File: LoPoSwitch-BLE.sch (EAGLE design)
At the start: 12 parts, among them Q1 2.5A/30V

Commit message: Restyle Board with SeedStudio Elements
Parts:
- removed C1, C2: 22uF, SparkFun-Capacitors:22UF-16V-20%-(1210)
- removed FREQ_RESONATOR: 16MHZ, SparkFun-FreqCtrl:RESONATOR16MHZ
- removed Q1: 2.5A/30V, SparkFun-DiscreteSemi:MOSFET-PCHANNELDMG2307L
- removed RESET.BUTTON: BUTTON-CONDUCTIVESMD, SparkFun-Electromechanical:BUTTON-CONDUCTIVESMD
- removed U$2: RELAY-2G5Q, SparkFun-Electromechanical:RELAY-2G5Q
- added CAPACITOR-16HZ: 16MHZ, Seeed-Crystal Oscillator:DIP-CRYSTAL-16MHZ-18PF-30PPM-50R(HC49US)
- added CAPACITOR-22PF-1, CAPACITOR-22PF-2, CAPACITOR-22PF-3, CAPACITOR-22PF-4: 100uf, Seeed-Capacitor:DIP-ALUMINUM-47UF-16V(D5-H7MM)
- added D1: 504BW, Seeed-LED:DIP-LED-BLUE-BLUE(2P-D5MM)
- added K1: (no value), Seeed-Relay:RELAY-HLS8L-DC5V-S-CHLS8L-DC5V-S-C
- added R1, R2, R6: 220R, Seeed-Resistor:DIP-RES-220R-5%-1/4W(PR-D2.3XL6.5MM)
- added R3: 1M, Seeed-Resistor:DIP-RES-1M-5%-1/4W(PR-D2.3XL6.5MM)
- added R4: 100K, Seeed-Resistor:DIP-RES-100K-5%-1/6W(PR-D1.8XL3.3MM)
- added RED-LED, RED-LED1: SR302DC, Seeed-LED:DIP-LED-RED-RED(2P-D3MM)
- added RESET-BUTTON: TS-1101F, Seeed-Switch:DIP-BUTTON(2P-6.0X3.0X4.3MM)-TS-1101F
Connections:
- removed net N$4: 12VO.1, Q1.S
- new net N$7: D1.+, R1.1
- new net N$8: R2.1, RED-LED.+
- new net N$9: ATMEGA328.P$22
- new net PD6: ATMEGA328.P$12, R6.1
- net 12VIN: now also 12VIN.2, K1.NO; no longer 12VIN.1, Q1.D
- net 3.3VIN: no longer C2.2
- net 5VIN: now also ATMEGA328.P$20, ATMEGA328.P$21, CAPACITOR-22PF-4.-, R2.2, R3.2; no longer C1.2
- net ARDUINO.D3: now also ATMEGA328.P$4; no longer Q1.G
- net GND: now also 12VIN.1, 12VO.1, ATMEGA328.P$10, ATMEGA328.P$9, RED-LED.-, RED-LED1.-, RESET-BUTTON.1; no longer 12VIN.2, 12VO.2, FREQ_RESONATOR.2, RESET.BUTTON.1
- net N$1: now also 12VO.2; no longer ATMEGA328.P$9, FREQ_RESONATOR.1
- net N$2: now also R6.2, RED-LED1.+; no longer ATMEGA328.P$10, FREQ_RESONATOR.3
- net N$3: now also RESET-BUTTON.2; no longer RESET.BUTTON.2
- net N$5: now also CAPACITOR-22PF-4.+; no longer C1.1
- net N$6: no longer C2.1
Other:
- moved on the sheet: 12VO

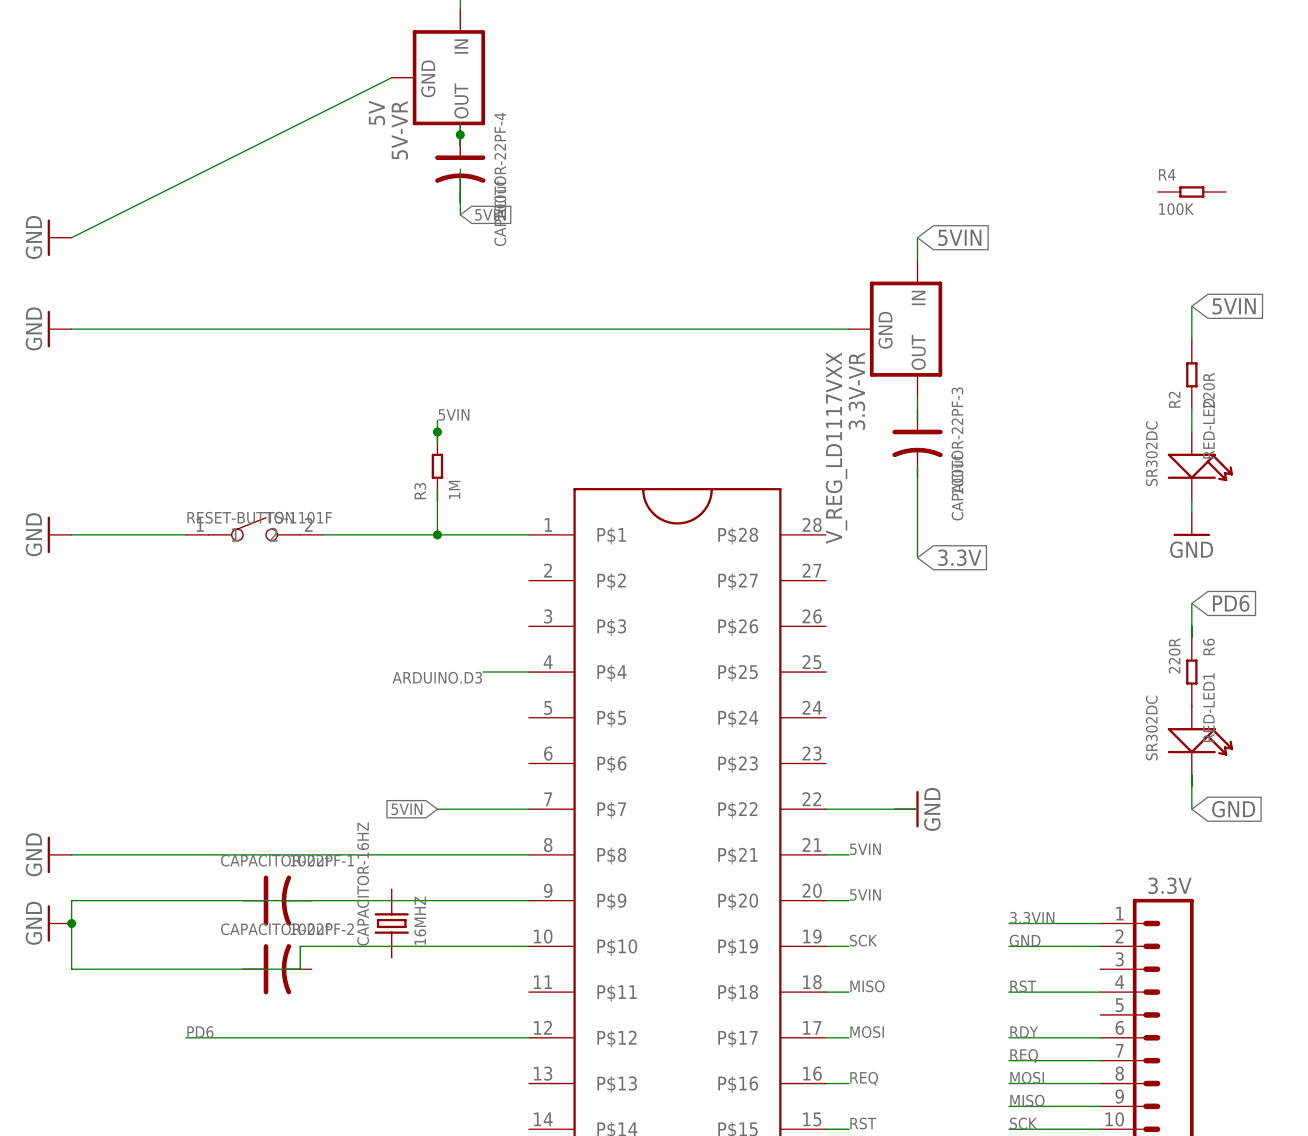
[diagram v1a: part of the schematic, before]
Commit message: Change Grid to 0.05 inch
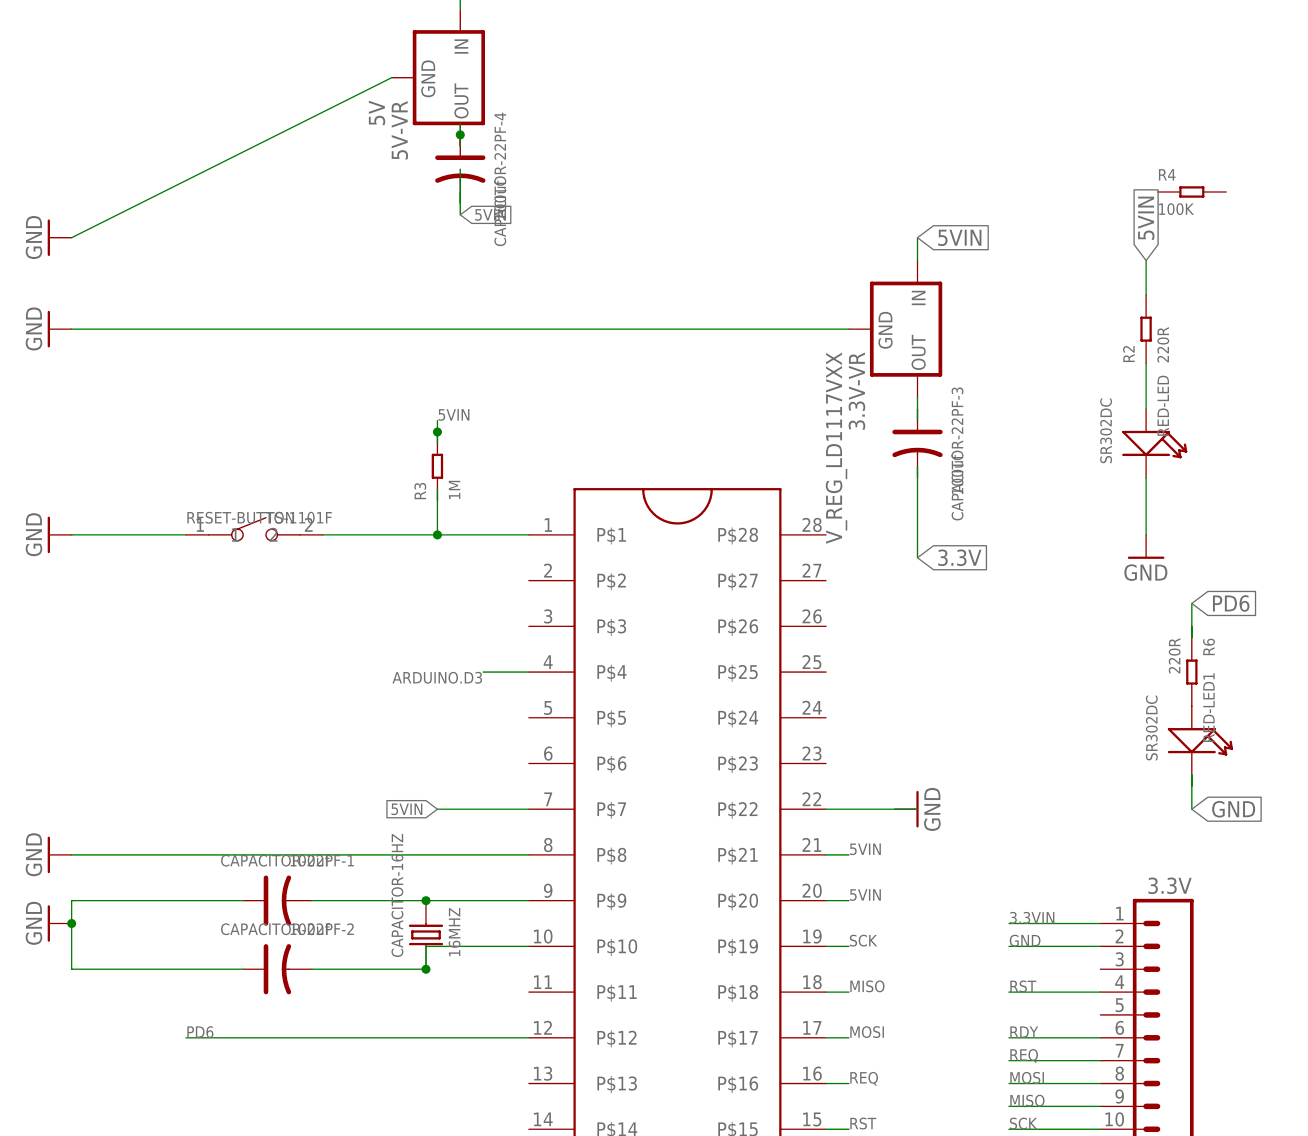
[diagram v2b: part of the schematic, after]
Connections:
- new net N$10: ATMEGA328.P$9, CAPACITOR-16HZ.2, CAPACITOR-22PF-1.-
- new net N$11: ATMEGA328.P$10, CAPACITOR-16HZ.1, CAPACITOR-22PF-2.-
- net GND: now also CAPACITOR-22PF-1.+, CAPACITOR-22PF-2.+; no longer ATMEGA328.P$10, ATMEGA328.P$9
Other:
- moved on the sheet: CAPACITOR-16HZ, R2, RED-LED
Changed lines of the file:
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@@
 <setting verticaltext="up"/>
 </settings>
-<grid distance="0.1" unitdist="inch" unit="inch" style="dots" multiple="1" display="yes" altdistance="0.01" altunitdist="inch" altunit="inch"/>
+<grid distance="0.05" unitdist="inch" unit="inch" style="lines" multiple="1" display="yes" altdistance="0.025" altunitdist="inch" altunit="inch"/>
 <layers>
 <layer number="1" name="Top" color="4" fill="1" visible="no" active="no"/>
@@
 <instance part="GND3" gate="1" x="119.38" y="-48.26" rot="R90"/>
 <instance part="GND8" gate="1" x="132.08" y="-111.76"/>
-<instance part="GND9" gate="1" x="149.86" y="-17.78"/>
+<instance part="GND9" gate="1" x="144.78" y="-20.32"/>
 <instance part="RESET-BUTTON" gate="G$1" x="45.72" y="-17.78"/>
-<instance part="CAPACITOR-16HZ" gate="G$1" x="60.96" y="-60.96" rot="R90"/>
+<instance part="CAPACITOR-16HZ" gate="G$1" x="64.77" y="-62.23" rot="R90"/>
 <instance part="CAPACITOR-22PF-1" gate="G$1" x="48.26" y="-58.42"/>
 <instance part="CAPACITOR-22PF-2" gate="G$1" x="48.26" y="-66.04"/>
 <instance part="CAPACITOR-22PF-3" gate="G$1" x="119.38" y="-7.62" rot="R270"/>
 <instance part="R6" gate="G$1" x="149.86" y="-33.02" rot="R270"/>
-<instance part="RED-LED" gate="G$1" x="149.86" y="-10.16" rot="R270"/>
+<instance part="RED-LED" gate="G$1" x="144.78" y="-7.62" rot="R270"/>
 <instance part="CAPACITOR-22PF-4" gate="G$1" x="68.58" y="22.86" rot="R270"/>
 <instance part="R3" gate="G$1" x="66.04" y="-10.16" rot="R90"/>
@@
 <instance part="GND11" gate="1" x="66.04" y="-124.46"/>
 <instance part="RED-LED1" gate="G$1" x="149.86" y="-40.64" rot="R270"/>
-<instance part="R2" gate="G$1" x="149.86" y="0" rot="R90"/>
+<instance part="R2" gate="G$1" x="144.78" y="5.08" rot="R90"/>
 <instance part="R4" gate="G$1" x="149.86" y="20.32"/>
 </instances>
@@
 </segment>
 <segment>
-<pinref part="ATMEGA328" gate="G$1" pin="P$9"/>
-<pinref part="GND2" gate="1" pin="GND"/>
-<wire x1="76.2" y1="-58.42" x2="25.4" y2="-58.42" width="0.1524" layer="91"/>
-<wire x1="25.4" y1="-58.42" x2="25.4" y2="-60.96" width="0.1524" layer="91"/>
-<pinref part="ATMEGA328" gate="G$1" pin="P$10"/>
-<wire x1="76.2" y1="-63.5" x2="50.8" y2="-63.5" width="0.1524" layer="91"/>
-<wire x1="50.8" y1="-63.5" x2="50.8" y2="-66.04" width="0.1524" layer="91"/>
-<wire x1="50.8" y1="-66.04" x2="25.4" y2="-66.04" width="0.1524" layer="91"/>
-<wire x1="25.4" y1="-66.04" x2="25.4" y2="-60.96" width="0.1524" layer="91"/>
-<junction x="25.4" y="-60.96"/>
-</segment>
-<segment>
 <pinref part="GND1" gate="1" pin="GND"/>
 <pinref part="12VO" gate="G$1" pin="1"/>
@@
 <pinref part="3.3V-VR" gate="G$1" pin="GND"/>
 <wire x1="25.4" y1="5.08" x2="111.76" y2="5.08" width="0.1524" layer="91"/>
-</segment>
-<segment>
-<pinref part="GND9" gate="1" pin="GND"/>
-<pinref part="RED-LED" gate="G$1" pin="-"/>
-<wire x1="149.86" y1="-13.97" x2="149.86" y2="-15.24" width="0.1524" layer="91"/>
 </segment>
 <segment>
@@
 <pinref part="RED-LED1" gate="G$1" pin="-"/>
 <wire x1="149.86" y1="-44.45" x2="149.86" y2="-45.72" width="0.1524" layer="91"/>
+</segment>
+<segment>
+<pinref part="RED-LED" gate="G$1" pin="-"/>
+<pinref part="GND9" gate="1" pin="GND"/>
+<wire x1="144.78" y1="-11.43" x2="144.78" y2="-17.78" width="0.1524" layer="91"/>
+</segment>
+<segment>
+<pinref part="CAPACITOR-22PF-1" gate="G$1" pin="+"/>
+<pinref part="GND2" gate="1" pin="GND"/>
+<wire x1="44.45" y1="-58.42" x2="25.4" y2="-58.42" width="0.1524" layer="91"/>
+<wire x1="25.4" y1="-58.42" x2="25.4" y2="-60.96" width="0.1524" layer="91"/>
+<pinref part="CAPACITOR-22PF-2" gate="G$1" pin="+"/>
+<wire x1="44.45" y1="-66.04" x2="25.4" y2="-66.04" width="0.1524" layer="91"/>
+<wire x1="25.4" y1="-66.04" x2="25.4" y2="-60.96" width="0.1524" layer="91"/>
+<junction x="25.4" y="-60.96"/>
 </segment>
 </net>
@@
 </segment>
 <segment>
-<wire x1="149.86" y1="7.62" x2="149.86" y2="3.81" width="0.1524" layer="91"/>
-<label x="149.86" y="7.62" size="1.778" layer="95" xref="yes"/>
 <pinref part="R2" gate="G$1" pin="2"/>
+<wire x1="144.78" y1="8.89" x2="144.78" y2="12.7" width="0.1524" layer="91"/>
+<label x="144.78" y="12.7" size="1.778" layer="95" rot="R90" xref="yes"/>
 </segment>
 </net>
@@
 </segment>
 </net>
-<net name="N$8" class="0">
-<segment>
-<pinref part="RED-LED" gate="G$1" pin="+"/>
-<pinref part="R2" gate="G$1" pin="1"/>
-<wire x1="149.86" y1="-3.81" x2="149.86" y2="-6.35" width="0.1524" layer="91"/>
-</segment>
-</net>
 <net name="N$2" class="0">
 <segment>
@@
 </segment>
 </net>
+<net name="N$8" class="0">
+<segment>
+<pinref part="R2" gate="G$1" pin="1"/>
+<pinref part="RED-LED" gate="G$1" pin="+"/>
+<wire x1="144.78" y1="1.27" x2="144.78" y2="-3.81" width="0.1524" layer="91"/>
+</segment>
+</net>
+<net name="N$10" class="0">
+<segment>
+<pinref part="ATMEGA328" gate="G$1" pin="P$9"/>
+<pinref part="CAPACITOR-16HZ" gate="G$1" pin="2"/>
+<wire x1="76.2" y1="-58.42" x2="64.77" y2="-58.42" width="0.1524" layer="91"/>
+<pinref part="CAPACITOR-22PF-1" gate="G$1" pin="-"/>
+<wire x1="64.77" y1="-58.42" x2="52.07" y2="-58.42" width="0.1524" layer="91"/>
+<junction x="64.77" y="-58.42"/>
+</segment>
+</net>
+<net name="N$11" class="0">
+<segment>
+<pinref part="ATMEGA328" gate="G$1" pin="P$10"/>
+<pinref part="CAPACITOR-16HZ" gate="G$1" pin="1"/>
+<wire x1="76.2" y1="-63.5" x2="64.77" y2="-63.5" width="0.1524" layer="91"/>
+<wire x1="64.77" y1="-63.5" x2="64.77" y2="-66.04" width="0.1524" layer="91"/>
+<pinref part="CAPACITOR-22PF-2" gate="G$1" pin="-"/>
+<wire x1="64.77" y1="-66.04" x2="52.07" y2="-66.04" width="0.1524" layer="91"/>
+<junction x="64.77" y="-66.04"/>
+</segment>
+</net>

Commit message: Generate Seed Gerber File
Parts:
- removed R4: 100K, Seeed-Resistor:DIP-RES-100K-5%-1/6W(PR-D1.8XL3.3MM)
- K1: value (none) -> 12V
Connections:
- removed net N$6: 3.3V-VR.OUT
- removed net N$9: ATMEGA328.P$22
- removed net PD6: ATMEGA328.P$12, R6.1
- removed net REQ: ATMEGA328.P$16, NRF8001.7
- new net ACT: NRF8001.5, NRF8001.7
- new net N$4: 3.3V-VR.OUT, CAPACITOR-22PF-3.+
- new net PIN13: ATMEGA328.P$15, R6.1
- net 12VIN: now also K1.V+; no longer K1.NO
- net 3.3VIN: now also CAPACITOR-22PF-3.-, NRF8001.3; no longer NRF8001.1
- net ARDUINO.D3: now also ATMEGA328.P$5, K1.NO; no longer ATMEGA328.P$4
- net GND: now also ATMEGA328.P$22, D1.-, K1.V-
- net N$1: now also K1.COM
- net N$3: now also R3.1
- net RDY: now also ATMEGA328.P$4
- net RST: now also ATMEGA328.P$16; no longer ATMEGA328.P$15
- net SCK: now also R1.2
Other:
- moved on the sheet: 5V-VR, R3

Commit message: some versione
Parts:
- removed 12VIN, 12VO: 12V, SparkFun-Connectors:M02JST-PTH-2
- removed 3.3V-VR: V_REG_LD1117VXX, SparkFun-PowerIC:V_REG_LD1117VXX
- removed 5V-VR: 5V, SparkFun-PowerIC:V_REG_78XX-TO-220
- removed CAPACITOR-22PF-3, CAPACITOR-22PF-4: 100uf, Seeed-Capacitor:DIP-ALUMINUM-47UF-16V(D5-H7MM)
- removed K1: 12V, Seeed-Relay:RELAY-HLS8L-DC5V-S-CHLS8L-DC5V-S-C
- added C1, C2: 0.1uF, rcl:C-EU075-052X106
- added C3, C5: 1uF, resistor:CPOL-US085CS-1AR
- added C4, C6: 10uF, resistor:CPOL-US085CS-1AR
- added D2, D3, D4, D5: 1N4002, diode:1N4004
- added IC3, IC4: LM317MB, Texas Instruments_By_element14_Batch_1:LM317MB
- added J1, J2: GREEN-2P-5.0, Seeed-Connector:SCREW-TERMINAL-GREEN(2P-5.0)
- added R4: 720Ω, resistor:R-US_M0805
- added R5: 240Ω, resistor:R-US_M0805
- added R7: 394Ω, resistor:R-US_M0805
- added REL1: Yellow, Opto:0044_KPT-2012YC
- added RL1: (no value), Rele':1045_G5V-2-H1
- added RN2: 1K, Resistenze:0005_064R_1K_/_CAY16-102J4LF
- added TR1: 2N7002, Transistors:1612_2N7002LT1G
- ATMEGA328, CAPACITOR-16HZ, NRF8001, R2, R3, R6, RED-LED, RED-LED1, RESET-BUTTON: OC_FARNELL (none) -> unknown
- CAPACITOR-22PF-1, CAPACITOR-22PF-2: value 100uf -> 22pf; OC_FARNELL (none) -> unknown
- D1: value 504BW -> 1N4148W; device Seeed-LED:DIP-LED-BLUE-BLUE(2P-D5MM) -> Diodi:0290_1N4148W; OC_FARNELL (none) -> unknown
- R1: value 220R -> 240Ω; device Seeed-Resistor:DIP-RES-220R-5%-1/4W(PR-D2.3XL6.5MM) -> resistor:R-US_M0805; OC_FARNELL (none) -> unknown
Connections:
- removed net N$7: D1.+, R1.1
- new net 12VO: J2.1, RL1.NO1, RL1.NO2
- new net N$14: D1.A, REL1.C, RL1.A1, TR1.D
- net 12VIN: now also C2.1, D2.C, IC3.IN, J1.1, RL1.C1, RL1.C2; no longer 12VIN.2, 5V-VR.IN, K1.V+
- net 3.3VIN: now also C5.+, D4.A, D5.C, IC4.OUT, R5.2; no longer CAPACITOR-22PF-3.-
- net 5VIN: now also C1.1, C3.+, D1.C, D2.A, D3.C, D4.C, IC3.OUT, IC4.IN, R1.2, RL1.A2, RN2A.2; no longer 3.3V-VR.IN, CAPACITOR-22PF-4.-
- net ARDUINO.D3: now also TR1.G; no longer K1.NO
- net GND: now also C1.2, C2.2, C3.-, C4.-, C5.-, C6.-, J1.2, J2.2, R4.1, R7.1, TR1.S; no longer 12VIN.1, 12VO.1, 3.3V-VR.GND, 5V-VR.GND, D1.-, K1.V-
- net N$1: now also C4.+, D3.A, IC3.ADJ, R1.1, R4.2; no longer 12VO.2, K1.COM
- net N$4: now also C6.+, D5.A, IC4.ADJ, R5.1, R7.2; no longer 3.3V-VR.OUT, CAPACITOR-22PF-3.+
- net N$5: now also REL1.A, RN2A.1; no longer 5V-VR.OUT, CAPACITOR-22PF-4.+
- net SCK: no longer R1.2
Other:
- note added: "3.3V Voltage Regulator"
- note added: "3.3V, 500mA"
- note added: "3V to 40V DC"
- note added: "5V Voltage Regulator"
- note added: "5V, 500mA"
- note added: "C2 of 1 µF tantalum capacitor on the output helps to improve transient response"
- note added: "C3 helps in ripple rejection upto 15dB"
- note added: "D1 protect the device against input short circuit"
- note added: "D2 protect against output short circuit for capacitance discharging"
- note added: "Useful Notes"
- note added: "Vref = 1.25V"
